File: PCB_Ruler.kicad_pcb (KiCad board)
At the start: 2 copper layers, 100.5 x 27 mm, 99 parts, among them Q1 SOT23-3, Q10 SOT89, Q11 SOT886, Q12 SOT963, Q13 SSOP-16, Q14 SSOP-8, Q15 SOT1113, Q16 SOT665, Q17 SO-8, Q18 QFNx24, Q19 QFPx100_0.5, Q2 SOT23-5, Q20 QFPx32, Q21 QFPx32_0.8, Q22 QFPx100, Q23 SOIC, Q24 TSOP-48, Q25 BGA_DDR3, Q26 BGA_10x, Q27 BGA_4x, Q28 QNFx20, Q29 QNFx40, Q3 SOT323, Q30 QNFx48, Q31 QNFx64, Q32 QFPx48, Q33 QFPx64, Q4 SOT353, Q5 SOT553, Q6 DPAK, Q7 DP2AK, Q8 LFPAK, Q9 SOT223, U1 1.00, U10 5mm, U11 6mm, U12 7mm, U13 8mm, U14 9mm, U15 3_10in, U16 0_16in, U17 1_16in, U18 2_16in, U19 3_16in, U2 1.27, U20 0_10in, U21 1_10in, U22 2_10in, U3 2.00, U4 2.54, U5 0mm, U6 1mm, U7 2mm, U8 3mm, U9 4mm

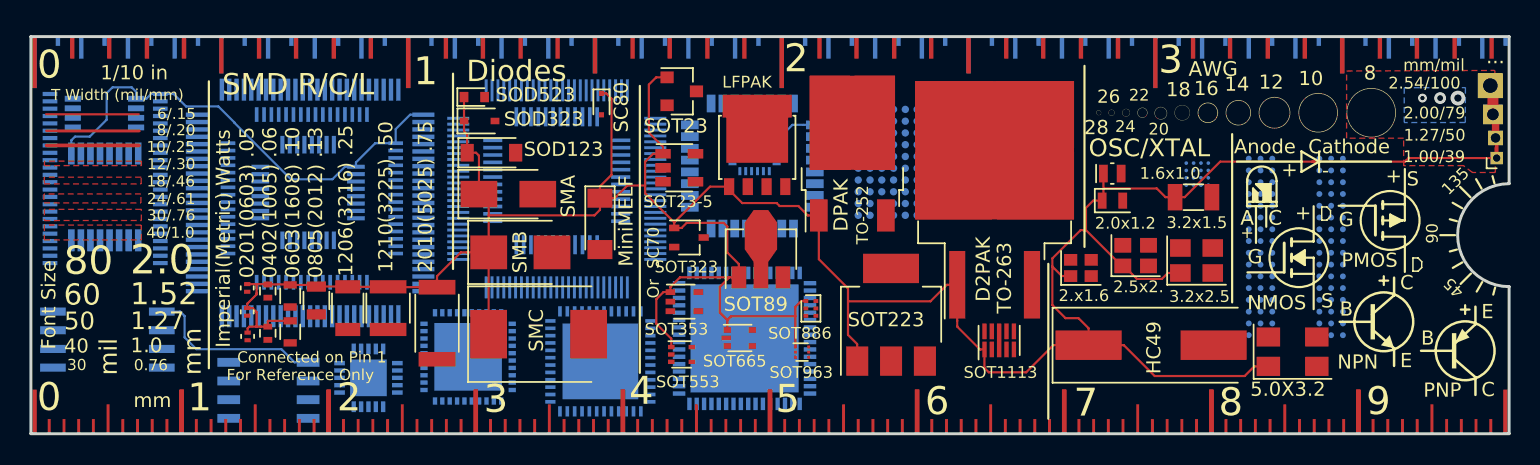
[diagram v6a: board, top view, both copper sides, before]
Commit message: Finished pad placement for redesign, still have a few more changes to do
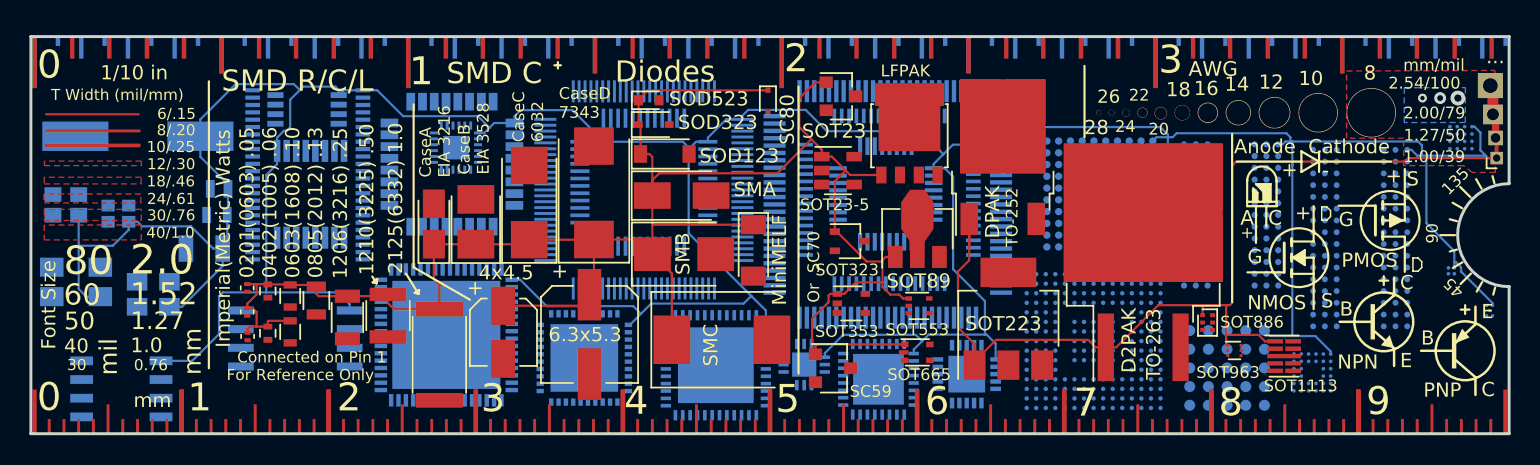
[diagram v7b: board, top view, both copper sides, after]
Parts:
- removed R11: R2010, Resistors_SMD:R_2010
- added C1: CP_4x4.5, Capacitors_SMD:CP_Elec_4x4.5, F.Cu at (102.1, 113.1)
- added C2: CP_6.3x5.3, Capacitors_SMD:CP_Elec_6.3x5.3, F.Cu at (108.0, 113.2)
- added C3: CaseB, Capacitors_Tantalum_SMD:CP_Tantalum_Case-B_EIA-3528-21_Reflow, F.Cu at (100.2, 105.6)
- added C4: CaseA, Capacitors_Tantalum_SMD:CP_Tantalum_Case-A_EIA-3216-18_Reflow, F.Cu at (97.4, 105.7)
- added C5: CaseC, Capacitors_Tantalum_SMD:CP_Tantalum_Case-C_EIA-6032-28_Reflow, F.Cu at (103.9, 104.3)
- added C6: CaseD, Capacitors_Tantalum_SMD:CP_Tantalum_Case-D_EIA-7343-31_Reflow, F.Cu at (108.3, 103.6)
- added Q34: BGA_5, Package_BGA:Texas_DSBGA-5_0.822x1.116mm_Layout2x1x2_P0.4mm, B.Cu at (169.2, 111.6)
- added Q35: BGA_78x, Package_BGA:FBGA-78_7.5x11mm_Layout2x3x13_P0.8mm, B.Cu at (151.6, 105.1)
- added Q36: BGA_4, Package_BGA:WLP-4_0.83x0.83mm_P0.4mm, B.Cu at (166.6, 108.9)
- added Q37: BGA_6x, Package_BGA:UFBGA-32_4.0x4.0mm_Layout6x6_P0.5mm, B.Cu at (157.1, 115.8)
- added Q38: BGA_5x_1.27, Package_BGA:BGA-25_6.35x6.35mm_Layout5x5_P1.27mm, B.Cu at (151.3, 115.5)
- added Q39: BGA_15x_0.65, Package_BGA:UFBGA-201_10x10mm_Layout15x15_P0.65mm, B.Cu at (142.2, 113.7)
- added Q40: QNFx32, Housings_DFN_QFN:QFN-32-1EP_5x5mm_Pitch0.5mm, B.Cu at (127.6, 116.3)
- added Q41: QNFx12, Housings_DFN_QFN:QFN-12-1EP_3x3mm_Pitch0.5mm, B.Cu at (122.6, 115.3)
- added Q42: SC-59, TO_SOT_Packages_SMD:SC-59, F.Cu at (124.5, 115.5)
- added R12: R2512, Resistors_SMD:R_2512, F.Cu at (97.8, 114.6)
- Q25: value BGA_DDR3 -> BGA_DDR4
- XT1, XT2, XT3, XT4, XT5, XT6, XT7, XT8: moved to B.Cu
- moved XT6 82.8 mm to (73.1, 109.7), turned to 180 degrees
- moved XT7 72.8 mm to (72.4, 104.4), turned to 180 degrees
- moved XT5 71.0 mm to (78.3, 110.5), turned to 180 degrees
- moved XT1 70.3 mm to (77.3, 99.8), turned to 180 degrees
- moved XT8 67.3 mm to (81.8, 107.4), turned to 0 degrees
- moved XT4 65.5 mm to (76.0, 105.0), turned to 180 degrees
- moved XT3 60.9 mm to (82.7, 105.1), turned to 180 degrees
- moved XT2 60.7 mm to (82.8, 103.3), turned to 180 degrees
- moved Q28 40.7 mm to (133.6, 116.0)
- moved Q20 39.3 mm to (128.1, 103.7)
- moved Q33 39.3 mm to (128.4, 104.1)
- moved Q19 39.3 mm to (128.3, 104.4)
- moved Q12 29.4 mm to (151.8, 114.3)
- moved Q11 27.0 mm to (150.0, 112.4)
- moved Q21 20.4 mm to (98.6, 101.7)
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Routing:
- net /Pin1: track 271.0 -> 484.1 mm
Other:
- board text added: "2.x1.2"
- board text added: "2125(6332) 1.0"
- board text added: "4x4.5"
- board text added: "6.3x5.3"
- board text added: "BGA100 P0.65"
- board text added: "BGA100 P0.8"
- board text added: "BGA16 P0.5"
- board text added: "BGA25 P1.27"
- board text added: "BGA32 P0.5"
- board text added: "BGA4 P0.4"
- board text added: "BGA5 P0.4"
- board text added: "BGA78 P0.8"
- board text added: "BGA96 P0.8"
- board text added: "CaseA EIA 3216"
- board text added: "CaseB EIA 3528"
- board text added: "CaseC 6032"
- board text added: "CaseD 7343"
- board text added: "DDR4 RAM"
- board text added: "QFN x20"
- board text added: "QFN x48"
- board text added: "SC59"
- board text added: "SMD C"
- board text added: "x12"
- board text added: "x32"
- board text removed: "2.0x1.2"
- board text removed: "2010(5025) .75"
- board text removed: "BGA"
- board text removed: "BGA 20X20"
- board text removed: "x20"
- board text removed: "x48"

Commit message: v2 revision basically finalized
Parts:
- added JP1: Jumper, Jumper:SolderJumper-2_P1.3mm_Open_TrianglePad1.0x1.5mm, F.Cu at (135.6, 95.7)
- added TP1: TestPoint, Connectors_TestPoints:Test_Point_Pad_1.0x1.0mm, F.Cu at (138.2, 95.9)
- added TP2: TestPoint, Connectors_TestPoints:Test_Point_Pad_d1.0mm, F.Cu at (140.3, 98.3)
- added TP3: TestPoint, Connectors_TestPoints:Test_Point_Pad_2.0x2.0mm, F.Cu at (140.6, 96.0)
- moved Q23 3.03 mm to (77.8, 114.4)
- moved Q11 2.73 mm to (152.7, 112.0)
- moved XT5 2.21 mm to (78.3, 108.3)
- moved Q6 1.56 mm to (136.0, 102.8)
- moved E$54 1.15 mm to (163.1, 112.7)
- moved Q15 1.14 mm to (156.3, 115.1)
- moved Q13 1.09 mm to (88.9, 102.6)
- moved Q14 1.09 mm to (88.7, 96.9)
- moved Q24 1.09 mm to (88.7, 101.3)
- moved Q16 1.09 mm to (129.2, 114.7)
- moved Q17 1.08 mm to (88.0, 112.4)
- moved Q9 1.07 mm to (136.3, 113.2)
- moved XT4 1.04 mm to (75.5, 104.1)
- moved XT6 0.94 mm to (73.1, 108.7)
- moved Q12 0.93 mm to (152.6, 114.9)
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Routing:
- net /Pin1: track 484.1 -> 486.3 mm
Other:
- board text added: "1 in = 2.54 mm"
- board text added: "1/10 cm"
- board text added: "F=(C*9/5)+32"
- board text added: "P=IV"
- board text added: "TP"
- board text added: "V=IR"
- board text added: "Z=sC"
- board text added: "Z=sL"
